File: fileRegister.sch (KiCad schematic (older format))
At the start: 12 parts

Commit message: Cleaning
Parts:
- gave numbers to parts that had none: 12
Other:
- moved on the sheet: C21, C22, C23, C25, C27, C29

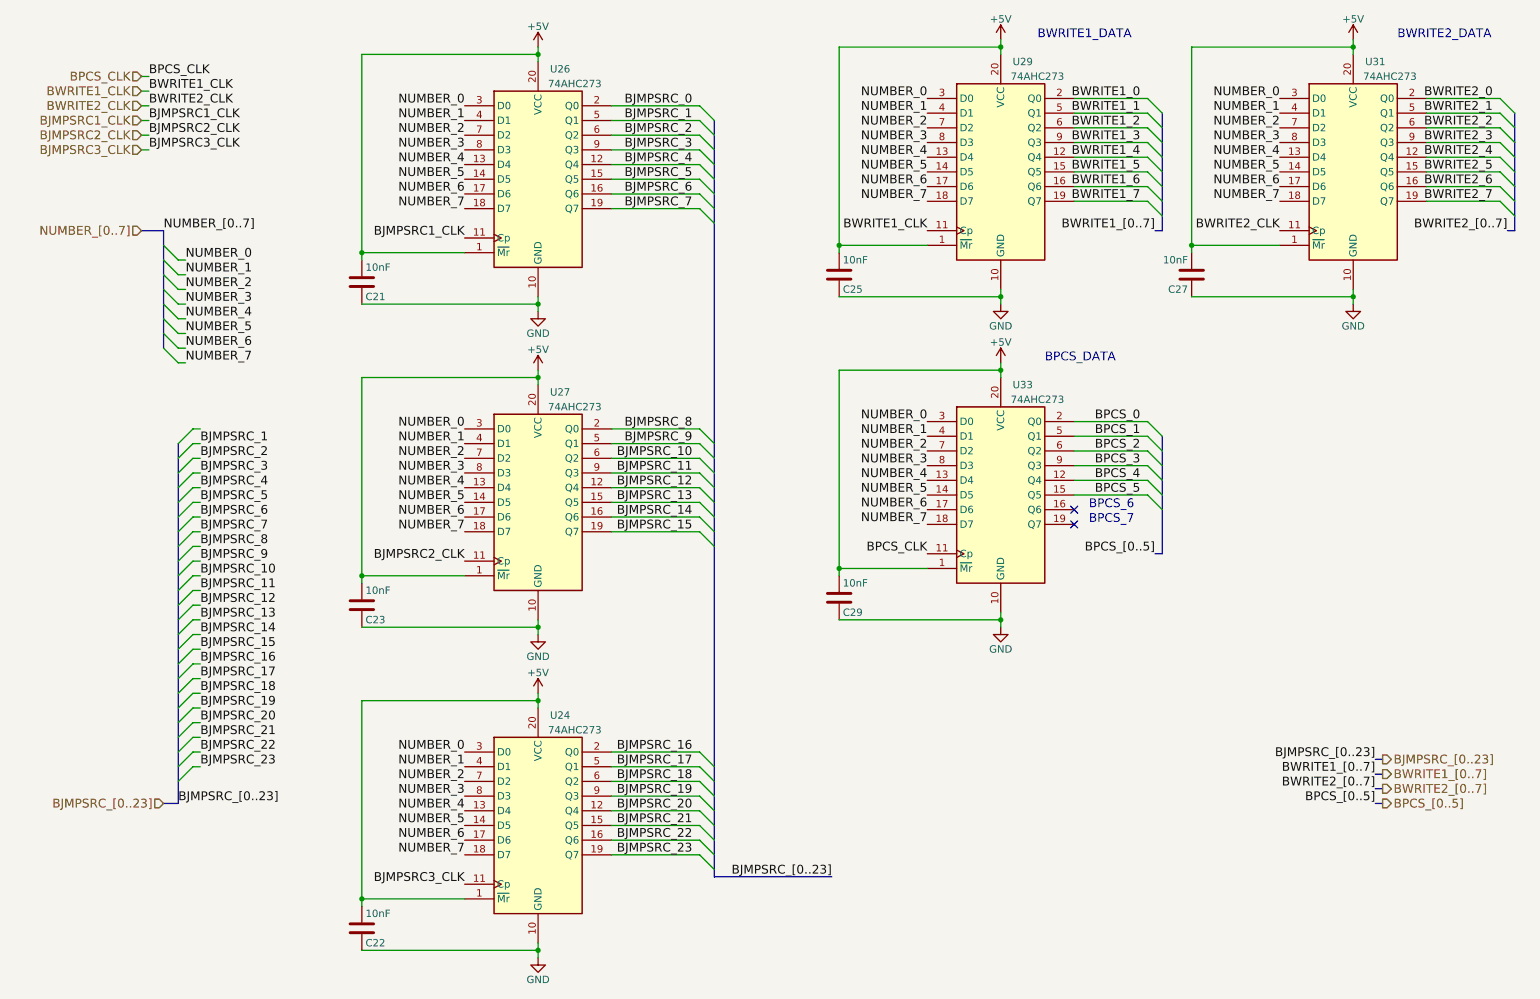
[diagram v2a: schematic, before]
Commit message: V5.1 (#9)
* Apply new symbol for XC2C256-VQ100 #5

* Set new date and 5.1

* Replacing 74HC165 with 74HC166, and add SPI_CFG_DS #4

* Replace some gates with a 74AHC1G02 to fix the pulse problem #3

* Go next only if SRCVALUE, (simple instruction)

* Remove weird ghost bus in register

* Small cleaning in fileRegister

* Go next only if SRCVALUE, (complex instruction) #8
adding 74AHC1G08

* Better decoupling #6

* Component association (#7)

* netlist

* Updated BOM for V5.1

* Routing, cleaning first pass

* bit of pcb cleaning

* SolderMaskClearance to 0

* Schematics to pdf

* PCB files in pdf

* exporting Gerbert files

* new 3d images

* Update README.md

* Modifying CHANGELOG file

* Update README.md
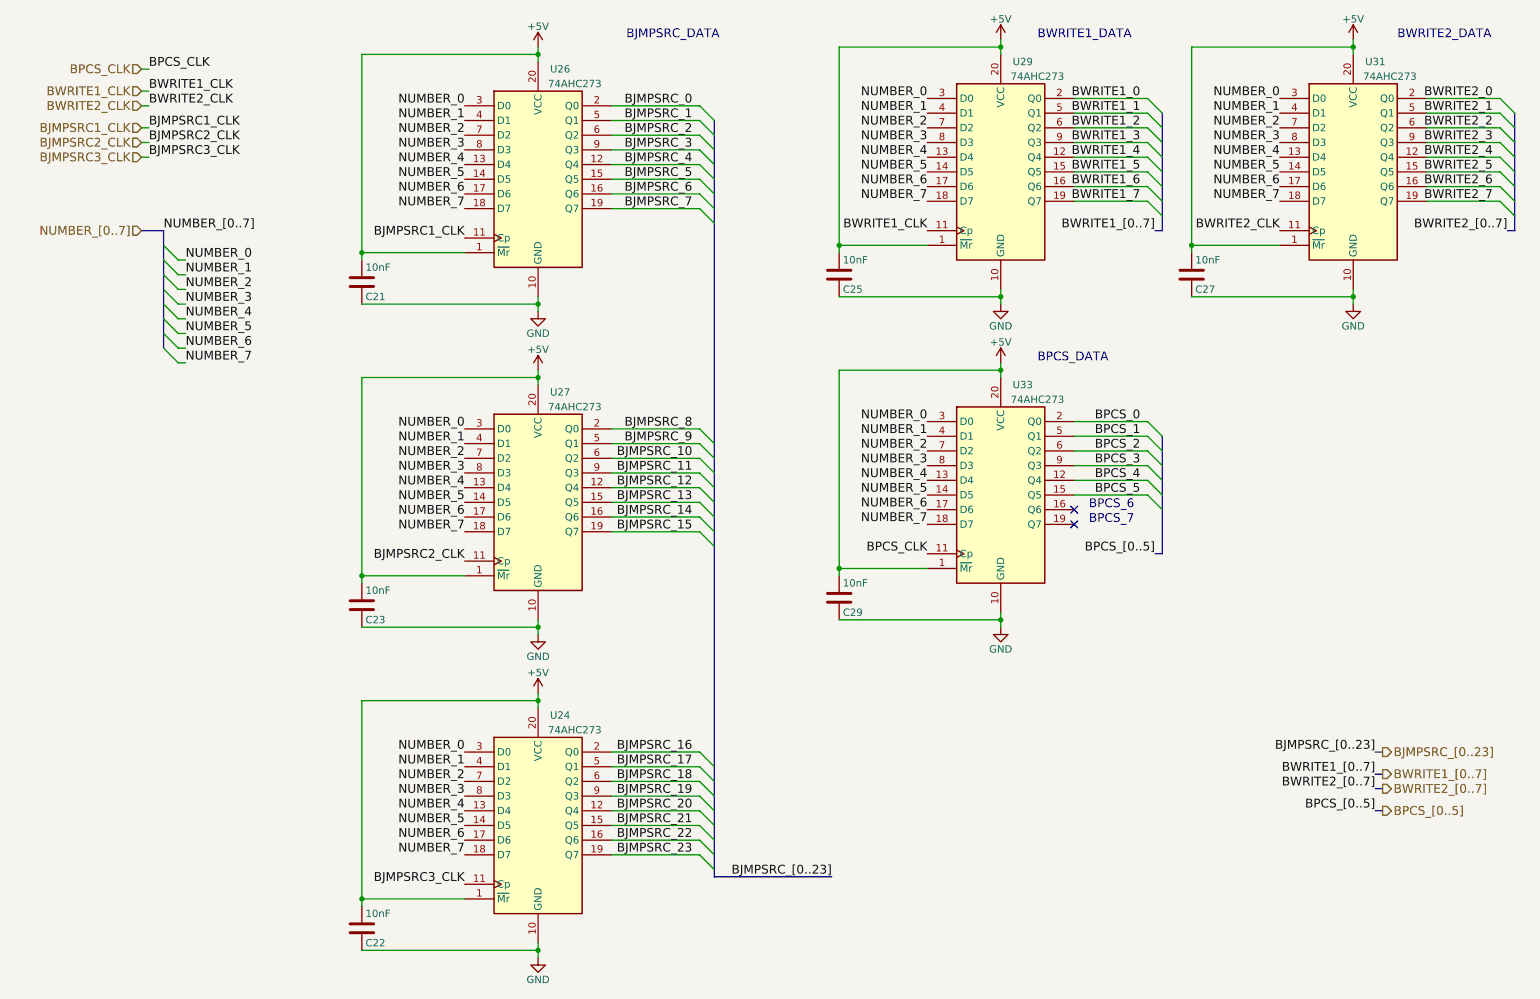
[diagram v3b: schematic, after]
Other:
- note added: "BJMPSRC_DATA"
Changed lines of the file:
@@
 Sheet 4 8
 Title "GP8B"
-Date "2020-08-19"
-Rev "V5.0"
+Date "2021-03-04"
+Rev "V5.1"
 Comp "Guillaume Guillet"
-Comment1 "Copyright Guillaume Guillet 2020"
+Comment1 "Copyright Guillaume Guillet 2021"
 Comment2 "Licensed under CERN-OHL-W v2 or later"
 Comment3 ""
@@
 F 3 "" H 8500 2450 50  0001 C CNN
 	1    8500 2450
-	-1   0    0    1
+	1    0    0    1
 $EndComp
 Text Notes 7450 850  0    60   ~ 0
@@
 	1    0    0    -1
 $EndComp
-Text Notes 7500 3050 0    60   ~ 0
+Text Notes 7450 3050 0    60   ~ 0
 BPCS_DATA
 Text Label 6700 1250 2    60   ~ 0
@@
 Text Label 1400 1300 0    60   ~ 0
 BWRITE2_CLK
-Text Label 1400 1100 0    60   ~ 0
+Text Label 1400 1050 0    60   ~ 0
 BPCS_CLK
-Text Label 1400 1400 0    60   ~ 0
+Text Label 1400 1450 0    60   ~ 0
 BJMPSRC1_CLK
-Text Label 1400 1500 0    60   ~ 0
+Text Label 1400 1550 0    60   ~ 0
 BJMPSRC2_CLK
-Text HLabel 1350 1100 0    60   Input ~ 0
+Text HLabel 1350 1050 0    60   Input ~ 0
 BPCS_CLK
 Text HLabel 1350 1200 0    60   Input ~ 0
@@
 Text HLabel 1350 1300 0    60   Input ~ 0
 BWRITE2_CLK
-Text HLabel 1350 1400 0    60   Input ~ 0
+Text HLabel 1350 1450 0    60   Input ~ 0
 BJMPSRC1_CLK
-Text HLabel 1350 1500 0    60   Input ~ 0
+Text HLabel 1350 1550 0    60   Input ~ 0
 BJMPSRC2_CLK
 Text HLabel 1350 2150 0    60   Input ~ 0
@@
 Entry Wire Line
 	5150 4200 5250 4300
-Text Label 1400 1600 0    60   ~ 0
+Text Label 1400 1650 0    60   ~ 0
 BJMPSRC3_CLK
-Text HLabel 1350 1600 0    60   Input ~ 0
+Text HLabel 1350 1650 0    60   Input ~ 0
 BJMPSRC3_CLK
 Text Label 1500 2150 0    60   ~ 0
@@
 Wire Bus Line
 	8300 4350 8250 4350
-Text Label 9750 6050 2    60   ~ 0
+Text Label 9750 6100 2    60   ~ 0
 BPCS_[0..5]
-Text HLabel 9800 6050 2    60   Output ~ 0
+Text HLabel 9800 6100 2    60   Output ~ 0
 BPCS_[0..5]
 Text HLabel 9800 5850 2    60   Output ~ 0
@@
 Text Label 9750 5950 2    60   ~ 0
 BWRITE2_[0..7]
-Text HLabel 9800 5750 2    60   Output ~ 0
+Text HLabel 9800 5700 2    60   Output ~ 0
 BJMPSRC_[0..23]
 Wire Wire Line
-	1350 1100 1400 1100
+	1350 1050 1400 1050
 Wire Wire Line
 	1350 1200 1400 1200
@@
 	1350 1300 1400 1300
 Wire Wire Line
-	1350 1400 1400 1400
-Wire Wire Line
-	1350 1500 1400 1500
-Wire Wire Line
-	1350 1600 1400 1600
-Wire Bus Line
-	9750 6050 9800 6050
-Wire Bus Line
-	9750 5750 9800 5750
+	1350 1450 1400 1450
+Wire Wire Line
+	1350 1550 1400 1550
+Wire Wire Line
+	1350 1650 1400 1650
+Wire Bus Line
+	9750 6100 9800 6100
+Wire Bus Line
+	9750 5700 9800 5700
 Wire Bus Line
 	9750 5850 9800 5850
@@
 Text Label 9100 2150 2    60   ~ 0
 BWRITE2_CLK
-Entry Wire Line
-	1700 4600 1600 4700
-Entry Wire Line
-	1700 4700 1600 4800
-Entry Wire Line
-	1700 4800 1600 4900
-Entry Wire Line
-	1700 4900 1600 5000
-Entry Wire Line
-	1700 5000 1600 5100
-Entry Wire Line
-	1700 5100 1600 5200
-Entry Wire Line
-	1700 5200 1600 5300
-Entry Wire Line
-	1700 5300 1600 5400
-Entry Wire Line
-	1700 5400 1600 5500
-Entry Wire Line
-	1700 5500 1600 5600
-Entry Wire Line
-	1700 5600 1600 5700
-Entry Wire Line
-	1700 5700 1600 5800
-Entry Wire Line
-	1700 5800 1600 5900
-Entry Wire Line
-	1700 3800 1600 3900
-Entry Wire Line
-	1700 3900 1600 4000
-Entry Wire Line
-	1700 4000 1600 4100
-Entry Wire Line
-	1700 4100 1600 4200
-Entry Wire Line
-	1700 4200 1600 4300
-Entry Wire Line
-	1700 4300 1600 4400
-Entry Wire Line
-	1700 4400 1600 4500
-Entry Wire Line
-	1700 4500 1600 4600
-Text Label 1600 6050 0    60   ~ 0
-BJMPSRC_[0..23]
-Entry Wire Line
-	1700 3500 1600 3600
-Entry Wire Line
-	1700 3600 1600 3700
-Entry Wire Line
-	1700 3700 1600 3800
-Wire Wire Line
-	1750 3500 1700 3500
-Wire Wire Line
-	1750 3600 1700 3600
-Wire Wire Line
-	1750 3700 1700 3700
-Wire Wire Line
-	1750 3800 1700 3800
-Wire Wire Line
-	1750 3900 1700 3900
-Wire Wire Line
-	1750 4000 1700 4000
-Wire Wire Line
-	1750 4100 1700 4100
-Wire Wire Line
-	1750 4200 1700 4200
-Wire Wire Line
-	1750 4300 1700 4300
-Wire Wire Line
-	1750 4400 1700 4400
-Wire Wire Line
-	1750 4500 1700 4500
-Wire Wire Line
-	1750 4600 1700 4600
-Wire Wire Line
-	1750 4700 1700 4700
-Wire Wire Line
-	1750 4800 1700 4800
-Wire Wire Line
-	1750 4900 1700 4900
-Wire Wire Line
-	1750 5000 1700 5000
-Wire Wire Line
-	1750 5100 1700 5100
-Wire Wire Line
-	1750 5200 1700 5200
-Wire Wire Line
-	1750 5300 1700 5300
-Wire Wire Line
-	1750 5400 1700 5400
-Wire Wire Line
-	1750 5500 1700 5500
-Wire Wire Line
-	1750 5600 1700 5600
-Wire Wire Line
-	1750 5700 1700 5700
-Wire Wire Line
-	1750 5800 1700 5800
-Text HLabel 1500 6050 0    60   Input ~ 0
-BJMPSRC_[0..23]
-Wire Bus Line
-	1600 6050 1500 6050
-Text Label 1750 3600 0    60   ~ 0
-BJMPSRC_1
-Text Label 1750 3700 0    60   ~ 0
-BJMPSRC_2
-Text Label 1750 3800 0    60   ~ 0
-BJMPSRC_3
-Text Label 1750 3900 0    60   ~ 0
-BJMPSRC_4
-Text Label 1750 4000 0    60   ~ 0
-BJMPSRC_5
-Text Label 1750 4100 0    60   ~ 0
-BJMPSRC_6
-Text Label 1750 4200 0    60   ~ 0
-BJMPSRC_7
-Text Label 1750 4300 0    60   ~ 0
-BJMPSRC_8
-Text Label 1750 4400 0    60   ~ 0
-BJMPSRC_9
-Text Label 1750 4500 0    60   ~ 0
-BJMPSRC_10
-Text Label 1750 4600 0    60   ~ 0
-BJMPSRC_11
-Text Label 1750 4700 0    60   ~ 0
-BJMPSRC_12
-Text Label 1750 4800 0    60   ~ 0
-BJMPSRC_13
-Text Label 1750 4900 0    60   ~ 0
-BJMPSRC_14
-Text Label 1750 5000 0    60   ~ 0
-BJMPSRC_15
-Text Label 1750 5100 0    60   ~ 0
-BJMPSRC_16
-Text Label 1750 5200 0    60   ~ 0
-BJMPSRC_17
-Text Label 1750 5300 0    60   ~ 0
-BJMPSRC_18
-Text Label 1750 5400 0    60   ~ 0
-BJMPSRC_19
-Text Label 1750 5500 0    60   ~ 0
-BJMPSRC_20
-Text Label 1750 5600 0    60   ~ 0
-BJMPSRC_21
-Text Label 1750 5700 0    60   ~ 0
-BJMPSRC_22
-Text Label 1750 5800 0    60   ~ 0
-BJMPSRC_23
 Text Label 5100 1300 2    60   ~ 0
 BJMPSRC_0
@@
 Text Label 5100 6400 2    60   ~ 0
 BJMPSRC_23
-Text Label 9750 5750 2    60   ~ 0
+Text Label 9750 5700 2    60   ~ 0
 BJMPSRC_[0..23]
 Text Label 6700 4350 2    60   ~ 0
@@
 Wire Wire Line
 	8500 2600 9600 2600
+Text Notes 4650 850  0    60   ~ 0
+BJMPSRC_DATA
 Wire Bus Line
 	8300 3550 8300 4350
@@
 Wire Bus Line
 	5250 1400 5250 6550
-Wire Bus Line
-	1600 3600 1600 6050
 $EndSCHEMATC
